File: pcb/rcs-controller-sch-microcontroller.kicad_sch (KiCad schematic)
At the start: 33 parts, among them J4 Screw_Terminal_4_P3.50mm, J5 USB_C_Receptacle_USB2.0_14P, J6 Conn_01x03, Q2 SI7465DP-T1-E3, Q3 SI7465DP-T1-E3, Q4 PMV45EN2, Q5 PMV45EN2, SW1 SW_Push, U1 LSM6DSOX, U4 ESP32-S3-WROOM-1

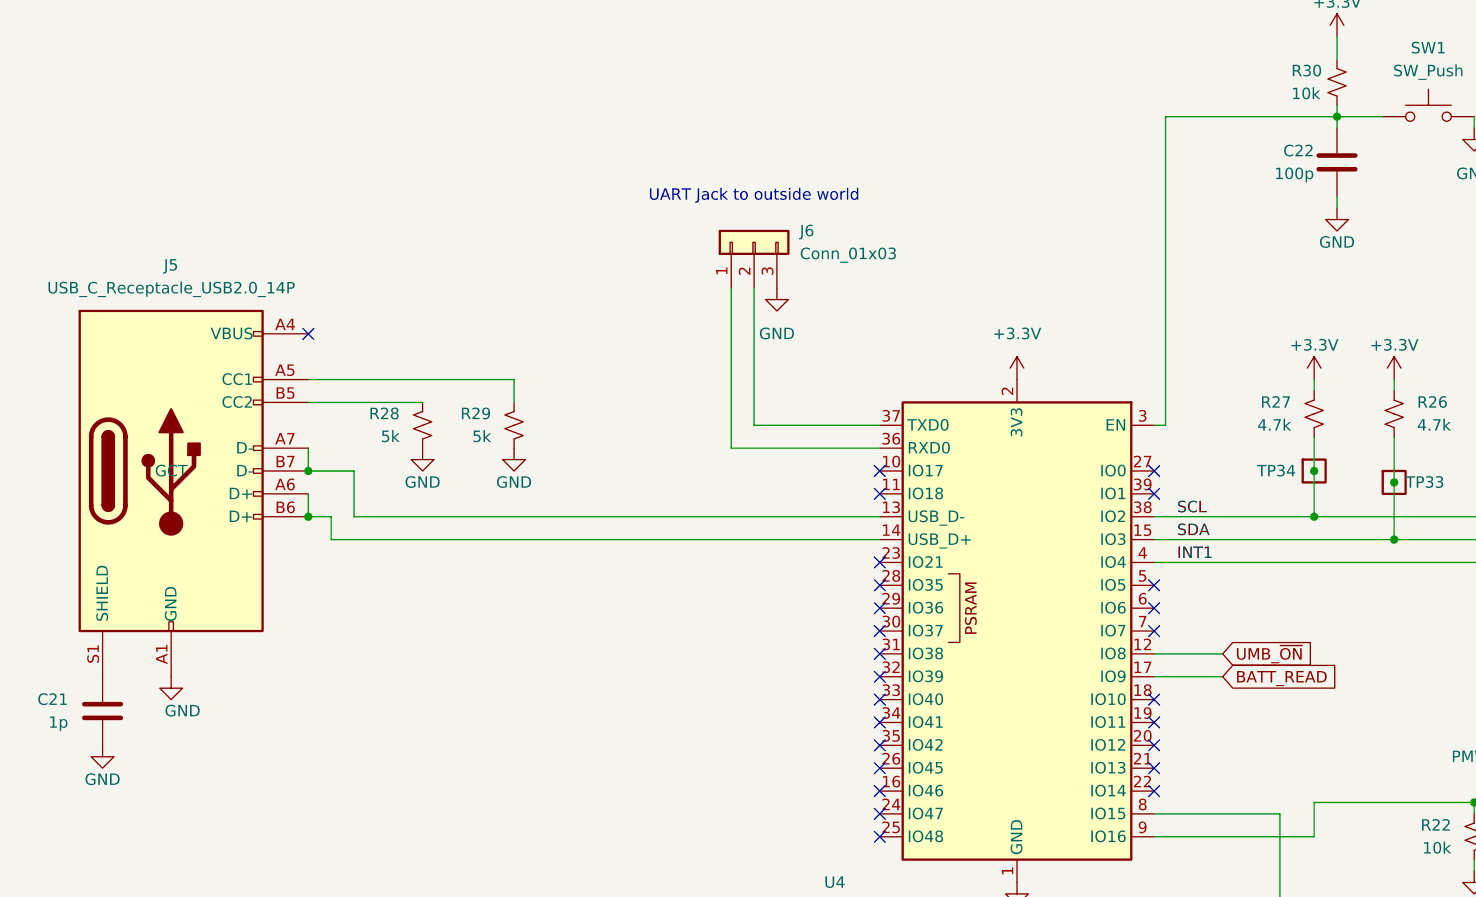
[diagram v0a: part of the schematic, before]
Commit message: Now with HTML BOM
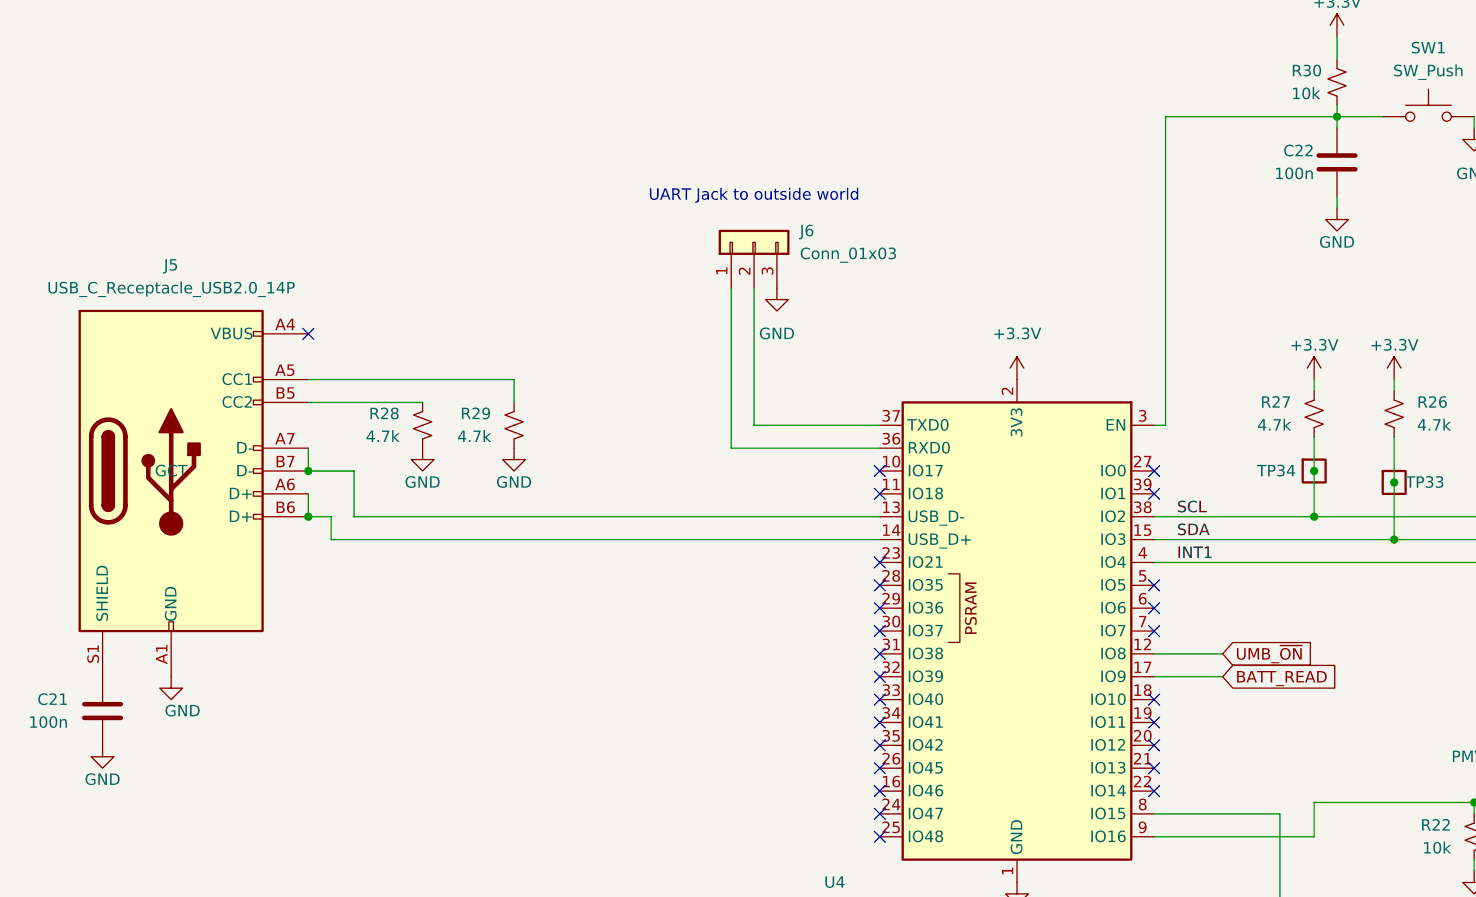
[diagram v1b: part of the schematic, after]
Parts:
- C21: value 1p -> 100n
- C22: value 100p -> 100n
- R28, R29: value 5k -> 4.7k; MPN RC0603FR-0710KL -> RC0603FR-074K7L
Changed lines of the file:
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@@
 			)
 		)
-		(property "Value" "5k"
+		(property "Value" "4.7k"
 			(at 138.43 114.2999 0)
 			(effects
@@
 			)
 		)
-		(property "MPN" "RC0603FR-0710KL"
+		(property "MPN" "RC0603FR-074K7L"
 			(at 140.97 113.03 0)
 			(effects
@@
 			)
 		)
-		(property "Value" "100p"
+		(property "Value" "100n"
 			(at 229.87 85.09 0)
 			(effects
@@
 			)
 		)
-		(property "Value" "1p"
+		(property "Value" "100n"
 			(at 91.44 146.0499 0)
 			(effects
@@
 			)
 		)
-		(property "Value" "5k"
+		(property "Value" "4.7k"
 			(at 128.27 114.2999 0)
 			(effects
@@
 			)
 		)
-		(property "MPN" "RC0603FR-0710KL"
+		(property "MPN" "RC0603FR-074K7L"
 			(at 130.81 113.03 0)
 			(effects
